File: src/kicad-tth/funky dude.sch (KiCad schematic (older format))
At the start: 33 parts, among them P1 CONN_2, P2 CONN_2, P3 CONN_2, SW1 SWITCH_INV, SW2 SWITCH_INV, U1 OP284

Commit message: 2014-10-12
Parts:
- C1, C13, C2, C4, C5: footprint Capacitors_ThroughHole:Capacitor7x2RM5 -> User:C2-LARGE_PADS
- C10, C12, C7, C8: footprint Capacitors_Elko_ThroughHole:Elko_vert_DM5_RM2-5_CopperClear -> User:C1V7-LARGE_PADS
- C11: footprint Capacitors_Elko_ThroughHole:Elko_vert_DM5_RM2-5_CopperClear -> User:C2-LARGE_PADS
- C3: value 11n -> 10n; footprint Capacitors_ThroughHole:Capacitor7x2RM5 -> User:C2-LARGE_PADS
- C6: value 50n -> 47n; footprint Capacitors_ThroughHole:Capacitor7x2RM5 -> User:C2-LARGE_PADS
- C9: value 47uf -> 47uF; footprint Capacitors_Elko_ThroughHole:Elko_vert_DM5_RM2-5_CopperClear -> User:C1V7-LARGE_PADS
- P1, P2, P3: footprint SIL-2-LARGE_PADS -> User:SIL-2-LARGE_PADS
- R1, R10, R11, R3, R5, R6, R7, R8, R9: footprint Discret:R3-LARGE_PADS -> User:R3-LARGE_PADS
- R2: value 500 -> 470; footprint Discret:R3-LARGE_PADS -> User:R3-LARGE_PADS
- R4: footprint Discret:R4-LARGE_PADS -> User:R4-LARGE_PADS
- RBASS1, RTREBLE1, SW1, SW2: footprint SIL-3-LARGE_PADS -> User:SIL-3-LARGE_PADS
- U1: footprint DIP-8_LARGE_PADS -> User:DIP-8_LARGE_PADS
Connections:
- wire segments 77 -> 101
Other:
- moved on the sheet: R3

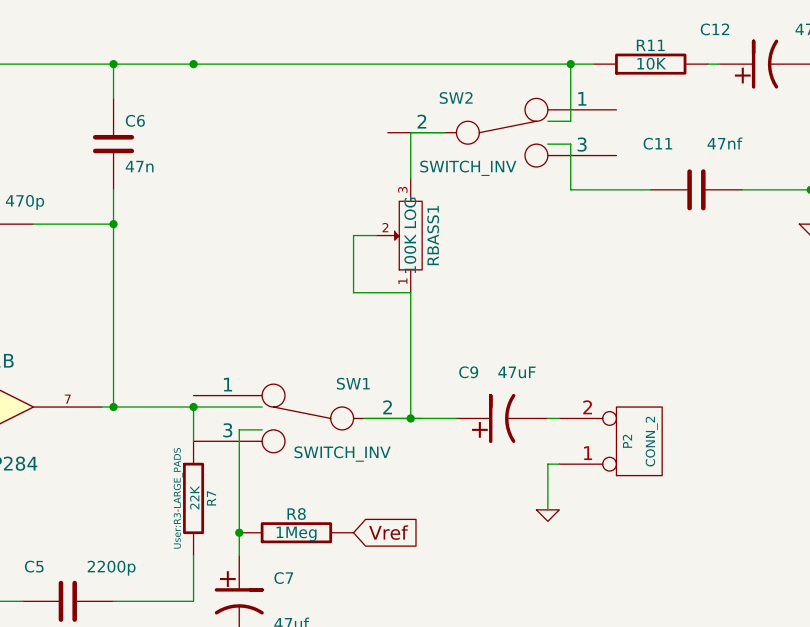
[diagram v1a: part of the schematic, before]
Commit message: changed switch to smaller symbol
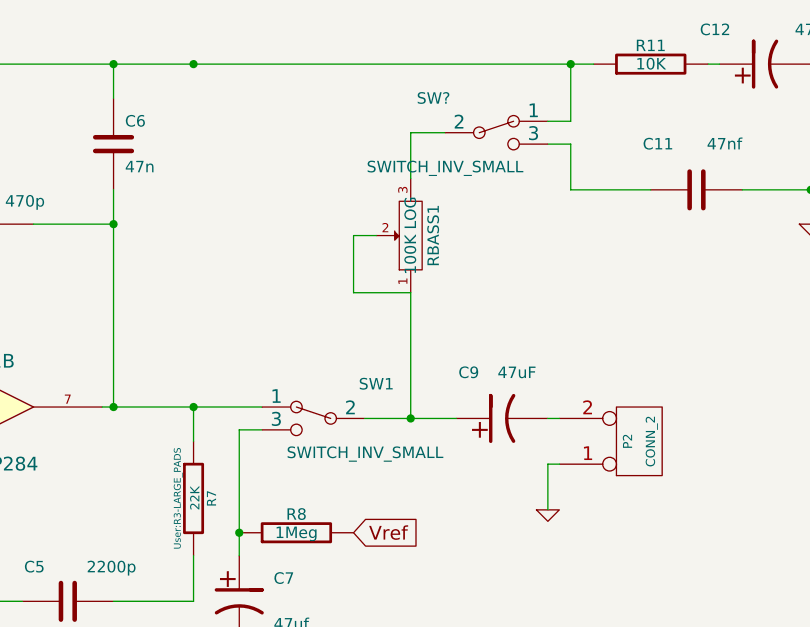
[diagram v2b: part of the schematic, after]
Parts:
- removed SW1, SW2: SWITCH_INV, User:SIL-3-LARGE_PADS, symbol SWITCH_INV
- added SW1, SW?: SWITCH_INV_SMALL, symbol SWITCH_INV_SMALL
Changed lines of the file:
@@
 Wire Wire Line
 	9200 2450 9500 2450
-$Comp
-L SWITCH_INV SW1
-U 1 1 51B1D3A0
-P 7300 3450
-F 0 "SW1" H 7100 3600 50  0000 C CNN
-F 1 "SWITCH_INV" H 7150 3300 50  0000 C CNN
-F 2 "User:SIL-3-LARGE_PADS" H 7300 3450 60  0001 C CNN
-F 3 "" H 7300 3450 60  0000 C CNN
-	1    7300 3450
-	-1   0    0    -1
-$EndComp
-$Comp
-L SWITCH_INV SW2
-U 1 1 51B1D3AF
-P 8150 2200
-F 0 "SW2" H 7950 2350 50  0000 C CNN
-F 1 "SWITCH_INV" H 8000 2050 50  0000 C CNN
-F 2 "User:SIL-3-LARGE_PADS" H 8150 2200 60  0001 C CNN
-F 3 "" H 8150 2200 60  0000 C CNN
-	1    8150 2200
-	1    0    0    -1
-$EndComp
 Wire Wire Line
 	8800 2450 8450 2450
@@
 	8350 3650 8400 3650
 Connection ~ 3400 3600
+$Comp
+L SWITCH_INV_SMALL SW?
+U 1 1 545E565F
+P 8150 2200
+F 0 "SW?" H 7850 2350 50  0000 C CNN
+F 1 "SWITCH_INV_SMALL" H 7900 2050 50  0000 C CNN
+F 2 "" H 8050 2200 60  0000 C CNN
+F 3 "" H 8050 2200 60  0000 C CNN
+	1    8150 2200
+	1    0    0    -1
+$EndComp
+$Comp
+L SWITCH_INV_SMALL SW1
+U 1 1 545E5692
+P 7300 3450
+F 0 "SW1" H 7000 3600 50  0000 C CNN
+F 1 "SWITCH_INV_SMALL" H 7050 3300 50  0000 C CNN
+F 2 "" H 7200 3450 60  0000 C CNN
+F 3 "" H 7200 3450 60  0000 C CNN
+	1    7300 3450
+	-1   0    0    -1
+$EndComp
 $EndSCHEMATC
